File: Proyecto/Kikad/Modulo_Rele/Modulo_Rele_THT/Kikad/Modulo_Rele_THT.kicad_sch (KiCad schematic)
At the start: 9 parts, among them J1 TB_1X3, J2 TB_1X3, K1 RELAY_C, Q1 BC337, U3 PC817

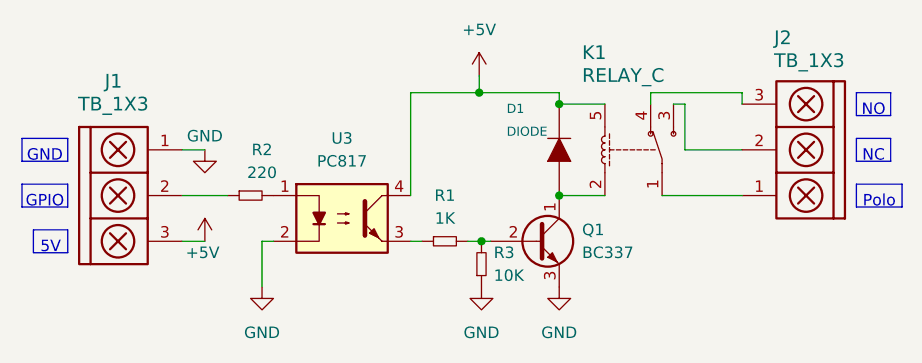
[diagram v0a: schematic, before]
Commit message: Agregue la carpeta Placa_Principal e hice unas correcciones en el Modulo_Rele
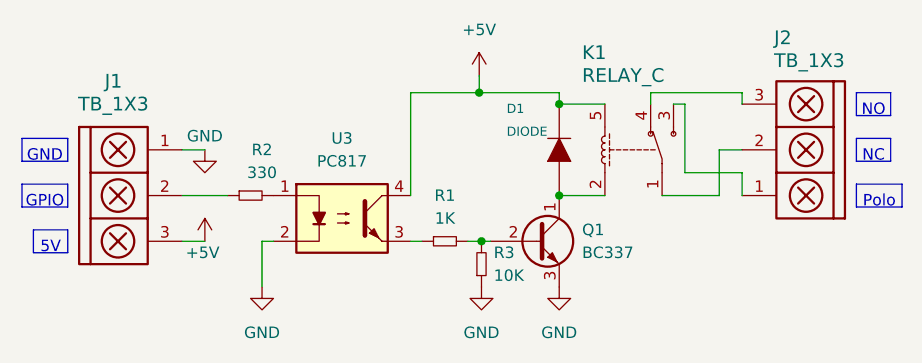
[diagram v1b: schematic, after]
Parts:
- J2: footprint Connector_Molex:Molex_KK-254_AE-6410-03A_1x03_P2.54mm_Vertical -> TerminalBlock:TerminalBlock_bornier-3_P5.08mm
- R2: value 220 -> 330
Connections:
- net at J2.1: now also K1.3; no longer K1.1
- net at J2.2: now also K1.1; no longer K1.3
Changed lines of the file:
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@@
 	(wire
 		(pts
-			(xy 160.02 73.66) (xy 168.91 73.66)
+			(xy 166.37 68.58) (xy 168.91 68.58)
 		)
 		(stroke
@@
 	(wire
 		(pts
+			(xy 166.37 73.66) (xy 166.37 68.58)
+		)
+		(stroke
+			(width 0)
+			(type default)
+		)
+	)
+	(wire
+		(pts
 			(xy 132.08 73.66) (xy 132.08 62.23)
 		)
@@
 	(wire
 		(pts
-			(xy 162.56 63.5) (xy 162.56 68.58)
-		)
-		(stroke
-			(width 0)
-			(type default)
-		)
-	)
-	(wire
-		(pts
-			(xy 162.56 68.58) (xy 168.91 68.58)
+			(xy 162.56 63.5) (xy 162.56 71.12)
+		)
+		(stroke
+			(width 0)
+			(type default)
+		)
+	)
+	(wire
+		(pts
+			(xy 168.91 71.12) (xy 162.56 71.12)
 		)
 		(stroke
@@
 	(wire
 		(pts
+			(xy 160.02 73.66) (xy 166.37 73.66)
+		)
+		(stroke
+			(width 0)
+			(type default)
+		)
+	)
+	(wire
+		(pts
 			(xy 139.7 60.325) (xy 139.7 62.23)
 		)
@@
 		(pts
 			(xy 115.57 78.74) (xy 116.84 78.74)
+		)
+		(stroke
+			(width 0)
+			(type default)
+		)
+	)
+	(wire
+		(pts
+			(xy 168.91 71.12) (xy 168.91 73.66)
 		)
 		(stroke
@@
 			)
 		)
-		(property "Footprint" "Connector_Molex:Molex_KK-254_AE-6410-03A_1x03_P2.54mm_Vertical"
+		(property "Footprint" "TerminalBlock:TerminalBlock_bornier-3_P5.08mm"
 			(at 185.42 54.102 0)
 			(effects
@@
 			)
 		)
-		(property "Value" "220"
+		(property "Value" "330"
 			(at 115.57 71.12 90)
 			(effects
